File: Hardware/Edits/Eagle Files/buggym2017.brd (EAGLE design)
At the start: 88.9 x 81.3 mm, 4 parts, among them IC3 BCC, IC4 L293E

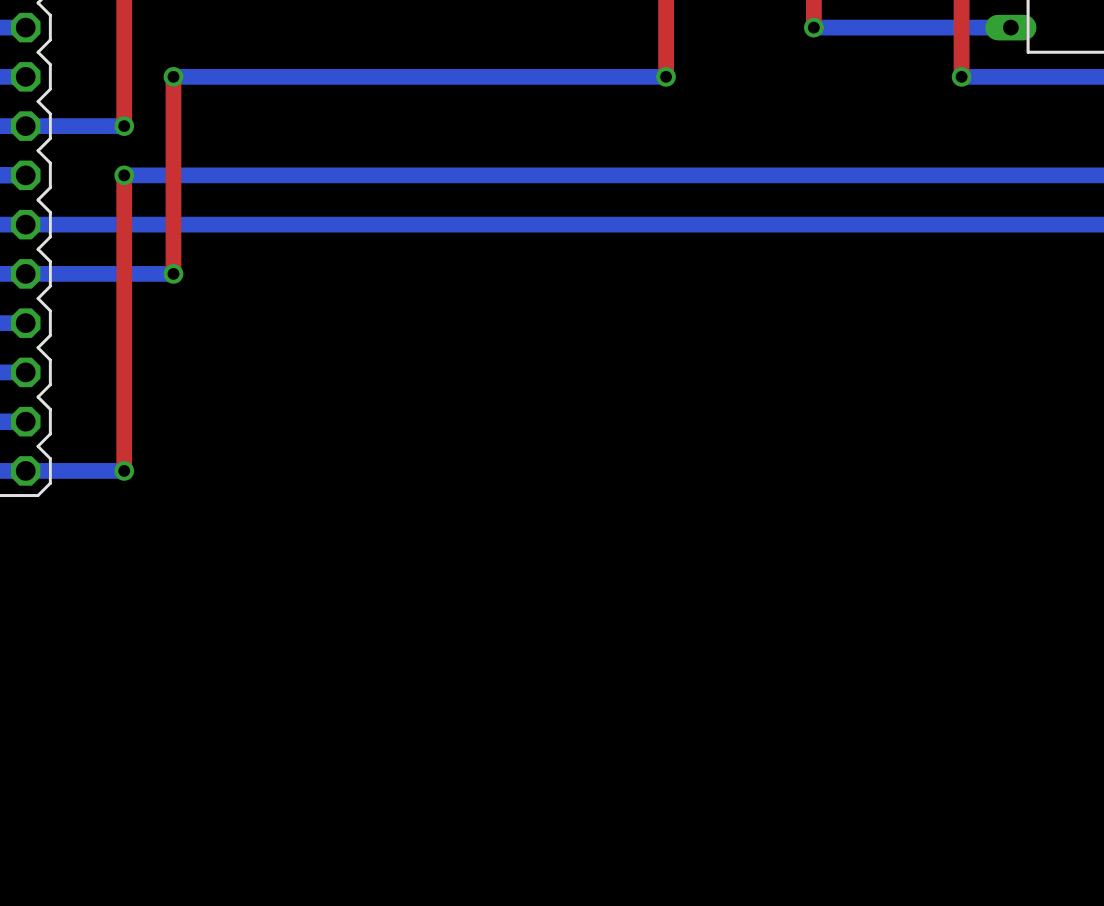
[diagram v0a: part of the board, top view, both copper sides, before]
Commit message: Tidy
Tidied up filesystem from HW Lab Week 3
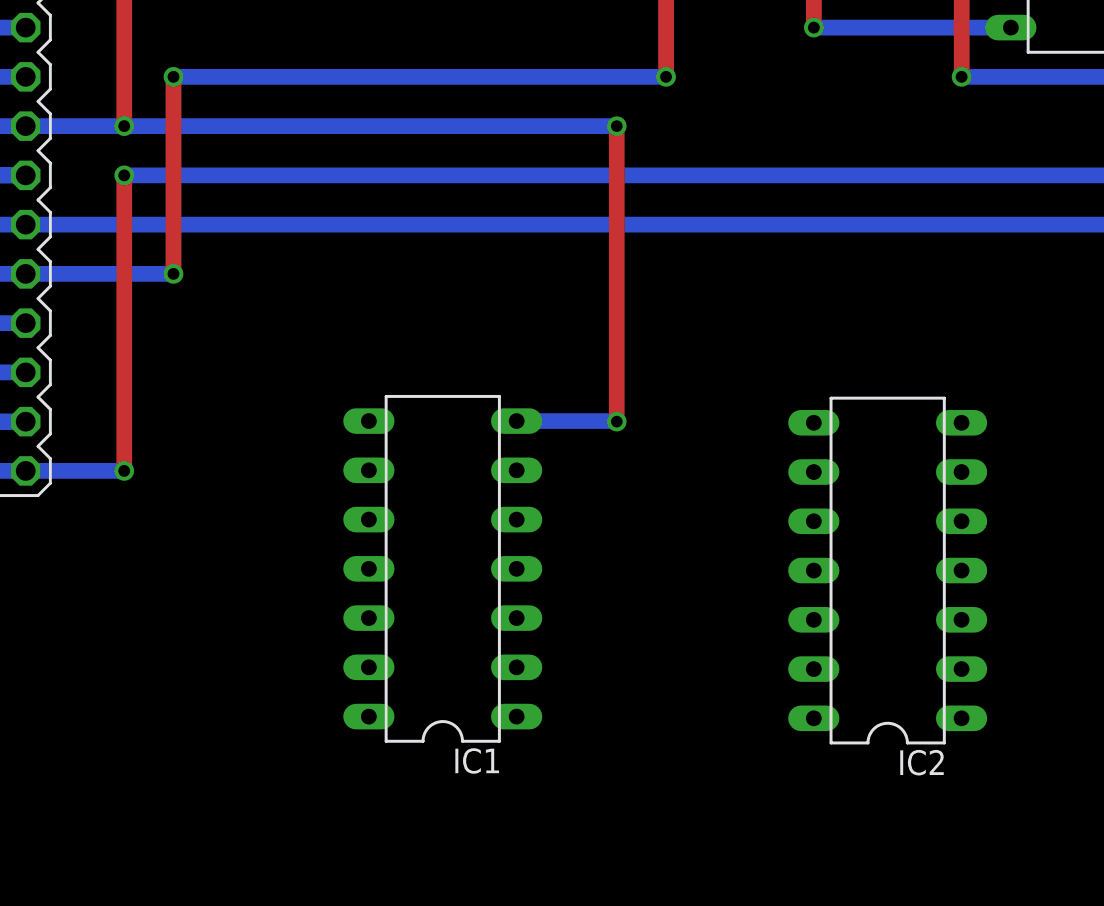
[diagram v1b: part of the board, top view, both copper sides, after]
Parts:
- added IC1: 4001N, 40xx:DIL14
- added IC2: 4075N, 40xx:DIL14
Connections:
- new net LM: IC2.9
- new net N$1: IC1.3, IC2.2
- new net N$4: IC1.4, IC2.4
- new net RM: IC2.6
- new net VDD: IC1.14, IC2.14
- net GND: now also IC1.7, IC2.7
- net L_EYE: now also BUGGY_CON.4
- net R_EYE: now also BUGGY_CON.3
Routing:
- net GND: track 94.0 -> 159.9 mm, vias 6 -> 8
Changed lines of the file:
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@@
 <?xml version="1.0" encoding="utf-8"?>
 <!DOCTYPE eagle SYSTEM "eagle.dtd">
-<eagle version="7.3.0">
+<eagle version="7.7.0">
 <drawing>
 <settings>
@@
 <setting verticaltext="up"/>
 </settings>
-<grid distance="0.1" unitdist="inch" unit="inch" style="lines" multiple="1" display="yes" altdistance="0.025" altunitdist="inch" altunit="inch"/>
+<grid distance="0.1" unitdist="inch" unit="inch" style="lines" multiple="1" display="yes" altdistance="0.01" altunitdist="inch" altunit="inch"/>
 <layers>
 <layer number="1" name="Top" color="4" fill="1" visible="yes" active="yes"/>
@@
 <layer number="27" name="tValues" color="7" fill="1" visible="yes" active="yes"/>
 <layer number="28" name="bValues" color="7" fill="1" visible="yes" active="yes"/>
-<layer number="29" name="tStop" color="7" fill="3" visible="no" active="yes"/>
-<layer number="30" name="bStop" color="7" fill="6" visible="no" active="yes"/>
-<layer number="31" name="tCream" color="7" fill="4" visible="no" active="yes"/>
-<layer number="32" name="bCream" color="7" fill="5" visible="no" active="yes"/>
-<layer number="33" name="tFinish" color="6" fill="3" visible="no" active="yes"/>
-<layer number="34" name="bFinish" color="6" fill="6" visible="no" active="yes"/>
-<layer number="35" name="tGlue" color="7" fill="4" visible="no" active="yes"/>
-<layer number="36" name="bGlue" color="7" fill="5" visible="no" active="yes"/>
-<layer number="37" name="tTest" color="7" fill="1" visible="no" active="yes"/>
-<layer number="38" name="bTest" color="7" fill="1" visible="no" active="yes"/>
+<layer number="29" name="tStop" color="7" fill="3" visible="yes" active="yes"/>
+<layer number="30" name="bStop" color="7" fill="6" visible="yes" active="yes"/>
+<layer number="31" name="tCream" color="7" fill="4" visible="yes" active="yes"/>
+<layer number="32" name="bCream" color="7" fill="5" visible="yes" active="yes"/>
+<layer number="33" name="tFinish" color="6" fill="3" visible="yes" active="yes"/>
+<layer number="34" name="bFinish" color="6" fill="6" visible="yes" active="yes"/>
+<layer number="35" name="tGlue" color="7" fill="4" visible="yes" active="yes"/>
+<layer number="36" name="bGlue" color="7" fill="5" visible="yes" active="yes"/>
+<layer number="37" name="tTest" color="7" fill="1" visible="yes" active="yes"/>
+<layer number="38" name="bTest" color="7" fill="1" visible="yes" active="yes"/>
 <layer number="39" name="tKeepout" color="4" fill="11" visible="yes" active="yes"/>
 <layer number="40" name="bKeepout" color="1" fill="11" visible="yes" active="yes"/>
@@
 <layer number="42" name="bRestrict" color="1" fill="10" visible="yes" active="yes"/>
 <layer number="43" name="vRestrict" color="2" fill="10" visible="yes" active="yes"/>
-<layer number="44" name="Drills" color="7" fill="1" visible="no" active="yes"/>
-<layer number="45" name="Holes" color="7" fill="1" visible="no" active="yes"/>
-<layer number="46" name="Milling" color="3" fill="1" visible="no" active="yes"/>
-<layer number="47" name="Measures" color="7" fill="1" visible="no" active="yes"/>
+<layer number="44" name="Drills" color="7" fill="1" visible="yes" active="yes"/>
+<layer number="45" name="Holes" color="7" fill="1" visible="yes" active="yes"/>
+<layer number="46" name="Milling" color="3" fill="1" visible="yes" active="yes"/>
+<layer number="47" name="Measures" color="7" fill="1" visible="yes" active="yes"/>
 <layer number="48" name="Document" color="7" fill="1" visible="yes" active="yes"/>
 <layer number="49" name="Reference" color="7" fill="1" visible="yes" active="yes"/>
@@
 </element>
 <element name="BUGGY_CON" library="2E10" package="2E10BOARD" value="2E10HDR" x="26.67" y="38.1"/>
+<element name="IC1" library="40xx" package="DIL14" value="4001N" x="49.44543125" y="17.810665625" rot="R90"/>
+<element name="IC2" library="40xx" package="DIL14" value="4075N" x="72.387890625" y="17.722265625" rot="R90"/>
 </elements>
 <signals>
@@
 <wire x1="27.94" y1="53.34" x2="43.18" y2="53.34" width="0.8128" layer="16"/>
 <via x="45.72" y="53.34" extent="1-16" drill="0.6096" shape="square"/>
+<contactref element="IC1" pad="7"/>
+<contactref element="IC2" pad="7"/>
+<wire x1="33.02" y1="40.64" x2="52.944703125" y2="40.64" width="0.4064" layer="16"/>
+<wire x1="52.944703125" y1="40.64" x2="52.944703125" y2="40.489321875" width="0.4064" layer="16"/>
+<wire x1="53.25543125" y1="25.430665625" x2="58.42" y2="25.430665625" width="0.8128" layer="16"/>
+<wire x1="58.42" y1="25.430665625" x2="58.42" y2="25.4" width="0.8128" layer="16"/>
+<via x="58.42" y="25.4" extent="1-16" drill="0.6" shape="square"/>
+<wire x1="58.42" y1="25.4" x2="58.42" y2="40.64" width="0.8128" layer="1"/>
+<via x="58.42" y="40.64" extent="1-16" drill="0.6" shape="square"/>
+<wire x1="58.42" y1="40.64" x2="33.02" y2="40.64" width="0.8128" layer="16"/>
+<wire x1="58.42" y1="25.430665625" x2="76.197890625" y2="25.342265625" width="0" layer="19" extent="16-16"/>
 </signal>
 <signal name="N$2">
@@
 <signal name="R_EYE">
 <contactref element="BUGGY_CON" pad="3'"/>
+<contactref element="BUGGY_CON" pad="3"/>
 </signal>
 <signal name="L_EYE">
 <contactref element="BUGGY_CON" pad="4'"/>
+<contactref element="BUGGY_CON" pad="4"/>
 </signal>
 <signal name="N$3">
@@
 <wire x1="60.96" y1="53.34" x2="58.42" y2="53.34" width="0.8128" layer="16"/>
 </signal>
+<signal name="VDD">
+<contactref element="IC1" pad="14"/>
+<contactref element="IC2" pad="14"/>
+<wire x1="45.63543125" y1="10.190665625" x2="68.577890625" y2="10.102265625" width="0" layer="19" extent="1-1"/>
+</signal>
+<signal name="N$1">
+<contactref element="IC1" pad="3"/>
+<contactref element="IC2" pad="2"/>
+<wire x1="53.25543125" y1="15.270665625" x2="76.197890625" y2="12.642265625" width="0" layer="19" extent="1-1"/>
+</signal>
+<signal name="LM">
+<contactref element="IC2" pad="9"/>
+</signal>
+<signal name="RM">
+<contactref element="IC2" pad="6"/>
+</signal>
+<signal name="N$4">
+<contactref element="IC1" pad="4"/>
+<contactref element="IC2" pad="4"/>
+<wire x1="53.25543125" y1="17.810665625" x2="76.197890625" y2="17.722265625" width="0" layer="19" extent="1-1"/>
+</signal>
 </signals>

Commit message: Work Done in Week 3  HardwareLab
Work done in Multisim and Eagle
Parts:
- removed IC1: 4001N, 40xx:DIL14
- removed IC2: 4075N, 40xx:DIL14
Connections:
- removed net LM: IC2.9
- removed net N$1: IC1.3, IC2.2
- removed net N$4: IC1.4, IC2.4
- removed net RM: IC2.6
- removed net VDD: IC1.14, IC2.14
- net GND: no longer IC1.7, IC2.7
- net L_EYE: no longer BUGGY_CON.4
- net R_EYE: no longer BUGGY_CON.3
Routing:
- net GND: track 159.9 -> 94.0 mm, vias 8 -> 6
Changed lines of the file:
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@@
 <?xml version="1.0" encoding="utf-8"?>
 <!DOCTYPE eagle SYSTEM "eagle.dtd">
-<eagle version="7.7.0">
+<eagle version="7.3.0">
 <drawing>
 <settings>
@@
 <setting verticaltext="up"/>
 </settings>
-<grid distance="0.1" unitdist="inch" unit="inch" style="lines" multiple="1" display="yes" altdistance="0.01" altunitdist="inch" altunit="inch"/>
+<grid distance="0.1" unitdist="inch" unit="inch" style="lines" multiple="1" display="yes" altdistance="0.025" altunitdist="inch" altunit="inch"/>
 <layers>
 <layer number="1" name="Top" color="4" fill="1" visible="yes" active="yes"/>
@@
 <layer number="27" name="tValues" color="7" fill="1" visible="yes" active="yes"/>
 <layer number="28" name="bValues" color="7" fill="1" visible="yes" active="yes"/>
-<layer number="29" name="tStop" color="7" fill="3" visible="yes" active="yes"/>
-<layer number="30" name="bStop" color="7" fill="6" visible="yes" active="yes"/>
-<layer number="31" name="tCream" color="7" fill="4" visible="yes" active="yes"/>
-<layer number="32" name="bCream" color="7" fill="5" visible="yes" active="yes"/>
-<layer number="33" name="tFinish" color="6" fill="3" visible="yes" active="yes"/>
-<layer number="34" name="bFinish" color="6" fill="6" visible="yes" active="yes"/>
-<layer number="35" name="tGlue" color="7" fill="4" visible="yes" active="yes"/>
-<layer number="36" name="bGlue" color="7" fill="5" visible="yes" active="yes"/>
-<layer number="37" name="tTest" color="7" fill="1" visible="yes" active="yes"/>
-<layer number="38" name="bTest" color="7" fill="1" visible="yes" active="yes"/>
+<layer number="29" name="tStop" color="7" fill="3" visible="no" active="yes"/>
+<layer number="30" name="bStop" color="7" fill="6" visible="no" active="yes"/>
+<layer number="31" name="tCream" color="7" fill="4" visible="no" active="yes"/>
+<layer number="32" name="bCream" color="7" fill="5" visible="no" active="yes"/>
+<layer number="33" name="tFinish" color="6" fill="3" visible="no" active="yes"/>
+<layer number="34" name="bFinish" color="6" fill="6" visible="no" active="yes"/>
+<layer number="35" name="tGlue" color="7" fill="4" visible="no" active="yes"/>
+<layer number="36" name="bGlue" color="7" fill="5" visible="no" active="yes"/>
+<layer number="37" name="tTest" color="7" fill="1" visible="no" active="yes"/>
+<layer number="38" name="bTest" color="7" fill="1" visible="no" active="yes"/>
 <layer number="39" name="tKeepout" color="4" fill="11" visible="yes" active="yes"/>
 <layer number="40" name="bKeepout" color="1" fill="11" visible="yes" active="yes"/>
@@
 <layer number="42" name="bRestrict" color="1" fill="10" visible="yes" active="yes"/>
 <layer number="43" name="vRestrict" color="2" fill="10" visible="yes" active="yes"/>
-<layer number="44" name="Drills" color="7" fill="1" visible="yes" active="yes"/>
-<layer number="45" name="Holes" color="7" fill="1" visible="yes" active="yes"/>
-<layer number="46" name="Milling" color="3" fill="1" visible="yes" active="yes"/>
-<layer number="47" name="Measures" color="7" fill="1" visible="yes" active="yes"/>
+<layer number="44" name="Drills" color="7" fill="1" visible="no" active="yes"/>
+<layer number="45" name="Holes" color="7" fill="1" visible="no" active="yes"/>
+<layer number="46" name="Milling" color="3" fill="1" visible="no" active="yes"/>
+<layer number="47" name="Measures" color="7" fill="1" visible="no" active="yes"/>
 <layer number="48" name="Document" color="7" fill="1" visible="yes" active="yes"/>
 <layer number="49" name="Reference" color="7" fill="1" visible="yes" active="yes"/>
@@
 </element>
 <element name="BUGGY_CON" library="2E10" package="2E10BOARD" value="2E10HDR" x="26.67" y="38.1"/>
-<element name="IC1" library="40xx" package="DIL14" value="4001N" x="49.44543125" y="17.810665625" rot="R90"/>
-<element name="IC2" library="40xx" package="DIL14" value="4075N" x="72.387890625" y="17.722265625" rot="R90"/>
 </elements>
 <signals>
@@
 <wire x1="27.94" y1="53.34" x2="43.18" y2="53.34" width="0.8128" layer="16"/>
 <via x="45.72" y="53.34" extent="1-16" drill="0.6096" shape="square"/>
-<contactref element="IC1" pad="7"/>
-<contactref element="IC2" pad="7"/>
-<wire x1="33.02" y1="40.64" x2="52.944703125" y2="40.64" width="0.4064" layer="16"/>
-<wire x1="52.944703125" y1="40.64" x2="52.944703125" y2="40.489321875" width="0.4064" layer="16"/>
-<wire x1="53.25543125" y1="25.430665625" x2="58.42" y2="25.430665625" width="0.8128" layer="16"/>
-<wire x1="58.42" y1="25.430665625" x2="58.42" y2="25.4" width="0.8128" layer="16"/>
-<via x="58.42" y="25.4" extent="1-16" drill="0.6" shape="square"/>
-<wire x1="58.42" y1="25.4" x2="58.42" y2="40.64" width="0.8128" layer="1"/>
-<via x="58.42" y="40.64" extent="1-16" drill="0.6" shape="square"/>
-<wire x1="58.42" y1="40.64" x2="33.02" y2="40.64" width="0.8128" layer="16"/>
-<wire x1="58.42" y1="25.430665625" x2="76.197890625" y2="25.342265625" width="0" layer="19" extent="16-16"/>
 </signal>
 <signal name="N$2">
@@
 <signal name="R_EYE">
 <contactref element="BUGGY_CON" pad="3'"/>
-<contactref element="BUGGY_CON" pad="3"/>
 </signal>
 <signal name="L_EYE">
 <contactref element="BUGGY_CON" pad="4'"/>
-<contactref element="BUGGY_CON" pad="4"/>
 </signal>
 <signal name="N$3">
@@
 <wire x1="60.96" y1="53.34" x2="58.42" y2="53.34" width="0.8128" layer="16"/>
 </signal>
-<signal name="VDD">
-<contactref element="IC1" pad="14"/>
-<contactref element="IC2" pad="14"/>
-<wire x1="45.63543125" y1="10.190665625" x2="68.577890625" y2="10.102265625" width="0" layer="19" extent="1-1"/>
-</signal>
-<signal name="N$1">
-<contactref element="IC1" pad="3"/>
-<contactref element="IC2" pad="2"/>
-<wire x1="53.25543125" y1="15.270665625" x2="76.197890625" y2="12.642265625" width="0" layer="19" extent="1-1"/>
-</signal>
-<signal name="LM">
-<contactref element="IC2" pad="9"/>
-</signal>
-<signal name="RM">
-<contactref element="IC2" pad="6"/>
-</signal>
-<signal name="N$4">
-<contactref element="IC1" pad="4"/>
-<contactref element="IC2" pad="4"/>
-<wire x1="53.25543125" y1="17.810665625" x2="76.197890625" y2="17.722265625" width="0" layer="19" extent="1-1"/>
-</signal>
 </signals>
